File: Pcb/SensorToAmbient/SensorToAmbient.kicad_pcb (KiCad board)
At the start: 2 copper layers, 161.9 x 69.7 mm, 17 parts, among them J1 Conn_01x04, J2 Conn_01x04, J3 Conn_01x04, J4 Conn_01x04, J5 Conn_01x04, J6 Conn_01x04, J7 Conn_01x02, J8 Conn_01x06, J9 Conn_01x06

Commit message: Commit intermediate (Delete Wil LTE outline from pcb)
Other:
- board size 161.9 x 69.7 mm -> 48.1 x 69.7 mm
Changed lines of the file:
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@@
   (general
     (thickness 1.6)
-    (drawings 18)
+    (drawings 10)
     (tracks 198)
     (zones 0)
@@
     (add_net GND)
   )
+  (module SensorToAmbient:RTC-8564NB_Akiduki (layer F.Cu)
+    (at 48.58 42.39)
+    (descr http://media.digikey.com/pdf/Data%20Sheets/Lite-On%20PDFs/6N137%20Series.pdf)
+    (fp_text reference RTC1 (at 4.05 -2.52) (layer F.SilkS)
+      (effects (font (size 1 1) (thickness 0.15)))
+    )
+    (fp_text value RTC-8564NB (at 3.94 12.954) (layer F.Fab)
+      (effects (font (size 1 1) (thickness 0.15)))
+    )
+    (fp_line (start -1.05 11.89) (end 8.67 11.89) (layer F.SilkS) (width 0.1))
+    (fp_line (start -1.05 -4.29) (end -1.05 11.89) (layer F.SilkS) (width 0.1))
+    (fp_line (start 8.67 -4.29) (end 8.67 11.89) (layer F.SilkS) (width 0.1))
+    (fp_line (start -1.05 -4.29) (end 8.67 -4.29) (layer F.SilkS) (width 0.1))
+    (fp_line (start 0.4 -0.9) (end 0.4 -1.2) (layer F.SilkS) (width 0.1))
+    (fp_line (start 0.4 -1.2) (end 0.7 -1.2) (layer F.SilkS) (width 0.1))
+    (fp_line (start 7.2 -0.9) (end 7.2 -1.2) (layer F.SilkS) (width 0.1))
+    (fp_line (start 7.2 -1.2) (end 6.9 -1.2) (layer F.SilkS) (width 0.1))
+    (fp_line (start 7.2 8.5) (end 7.2 8.8) (layer F.SilkS) (width 0.1))
+    (fp_line (start 7.2 8.8) (end 6.9 8.8) (layer F.SilkS) (width 0.1))
+    (fp_line (start 0.4 8.5) (end 0.4 8.8) (layer F.SilkS) (width 0.1))
+    (fp_line (start 0.4 8.8) (end 0.7 8.8) (layer F.SilkS) (width 0.1))
+    (fp_line (start 0.55 8.64) (end 7.05 8.64) (layer F.Fab) (width 0.1))
+    (fp_line (start 0.55 -1.04) (end 7.05 -1.04) (layer F.Fab) (width 0.1))
+    (fp_line (start 7.05 -1.04) (end 7.05 8.64) (layer F.Fab) (width 0.1))
+    (fp_line (start 0.55 -1.04) (end 0.55 8.64) (layer F.Fab) (width 0.1))
+    (fp_text user REF** (at 3.94 3.49) (layer F.Fab)
+      (effects (font (size 1 1) (thickness 0.1)))
+    )
+    (pad 1 thru_hole rect (at 0 0) (size 1.6 1.6) (drill 1) (layers *.Cu *.Mask)
+      (net 34 "Net-(RTC1-Pad1)"))
+    (pad 2 thru_hole circle (at 0 2.54) (size 1.6 1.6) (drill 1) (layers *.Cu *.Mask)
+      (net 16 "Net-(J2-Pad4)"))
+    (pad 3 thru_hole circle (at 0 5.08) (size 1.6 1.6) (drill 1) (layers *.Cu *.Mask)
+      (net 12 "Net-(DCDC1-Pad3)"))
+    (pad 4 thru_hole circle (at 0 7.62) (size 1.6 1.6) (drill 1) (layers *.Cu *.Mask)
+      (net 6 GND))
+    (pad 8 thru_hole circle (at 7.62 7.62) (size 1.6 1.6) (drill 1) (layers *.Cu *.Mask)
+      (net 19 /PWR_BAT))
+    (pad 7 thru_hole circle (at 7.62 5.08) (size 1.6 1.6) (drill 1) (layers *.Cu *.Mask)
+      (net 18 "Net-(RTC1-Pad7)"))
+    (pad 6 thru_hole circle (at 7.62 2.54) (size 1.6 1.6) (drill 1) (layers *.Cu *.Mask)
+      (net 20 "Net-(J5-Pad4)"))
+    (pad 5 thru_hole circle (at 7.62 0) (size 1.6 1.6) (drill 1) (layers *.Cu *.Mask)
+      (net 21 "Net-(J5-Pad3)"))
+    (model ${KIPRJMOD}/RTC-8564NB_Akidsuki.wrl
+      (at (xyz 0 0 0))
+      (scale (xyz 0.394 0.394 0.394))
+      (rotate (xyz -90 0 0))
+    )
+  )
   (module SensorToAmbient:DCDC_PowerBoost500 (layer F.Cu)
     (at 46.28 73.08 270)
@@
       (net 19 /PWR_BAT))
     (model ${KIPRJMOD}/PowerBoost500.wrl
-      (at (xyz 0 0 0))
-      (scale (xyz 0.394 0.394 0.394))
-      (rotate (xyz -90 0 0))
-    )
-  )
-  (module SensorToAmbient:RTC-8564NB_Akiduki (layer F.Cu)
-    (at 48.58 42.39)
-    (descr http://media.digikey.com/pdf/Data%20Sheets/Lite-On%20PDFs/6N137%20Series.pdf)
-    (fp_text reference RTC1 (at 4.05 -2.52) (layer F.SilkS)
-      (effects (font (size 1 1) (thickness 0.15)))
-    )
-    (fp_text value RTC-8564NB (at 3.94 12.954) (layer F.Fab)
-      (effects (font (size 1 1) (thickness 0.15)))
-    )
-    (fp_text user REF** (at 3.94 3.49) (layer F.Fab)
-      (effects (font (size 1 1) (thickness 0.1)))
-    )
-    (fp_line (start 0.55 -1.04) (end 0.55 8.64) (layer F.Fab) (width 0.1))
-    (fp_line (start 7.05 -1.04) (end 7.05 8.64) (layer F.Fab) (width 0.1))
-    (fp_line (start 0.55 -1.04) (end 7.05 -1.04) (layer F.Fab) (width 0.1))
-    (fp_line (start 0.55 8.64) (end 7.05 8.64) (layer F.Fab) (width 0.1))
-    (fp_line (start 0.4 8.8) (end 0.7 8.8) (layer F.SilkS) (width 0.1))
-    (fp_line (start 0.4 8.5) (end 0.4 8.8) (layer F.SilkS) (width 0.1))
-    (fp_line (start 7.2 8.8) (end 6.9 8.8) (layer F.SilkS) (width 0.1))
-    (fp_line (start 7.2 8.5) (end 7.2 8.8) (layer F.SilkS) (width 0.1))
-    (fp_line (start 7.2 -1.2) (end 6.9 -1.2) (layer F.SilkS) (width 0.1))
-    (fp_line (start 7.2 -0.9) (end 7.2 -1.2) (layer F.SilkS) (width 0.1))
-    (fp_line (start 0.4 -1.2) (end 0.7 -1.2) (layer F.SilkS) (width 0.1))
-    (fp_line (start 0.4 -0.9) (end 0.4 -1.2) (layer F.SilkS) (width 0.1))
-    (fp_line (start -1.05 -4.29) (end 8.67 -4.29) (layer F.SilkS) (width 0.1))
-    (fp_line (start 8.67 -4.29) (end 8.67 11.89) (layer F.SilkS) (width 0.1))
-    (fp_line (start -1.05 -4.29) (end -1.05 11.89) (layer F.SilkS) (width 0.1))
-    (fp_line (start -1.05 11.89) (end 8.67 11.89) (layer F.SilkS) (width 0.1))
-    (pad 5 thru_hole circle (at 7.62 0) (size 1.6 1.6) (drill 1) (layers *.Cu *.Mask)
-      (net 21 "Net-(J5-Pad3)"))
-    (pad 6 thru_hole circle (at 7.62 2.54) (size 1.6 1.6) (drill 1) (layers *.Cu *.Mask)
-      (net 20 "Net-(J5-Pad4)"))
-    (pad 7 thru_hole circle (at 7.62 5.08) (size 1.6 1.6) (drill 1) (layers *.Cu *.Mask)
-      (net 18 "Net-(RTC1-Pad7)"))
-    (pad 8 thru_hole circle (at 7.62 7.62) (size 1.6 1.6) (drill 1) (layers *.Cu *.Mask)
-      (net 19 /PWR_BAT))
-    (pad 4 thru_hole circle (at 0 7.62) (size 1.6 1.6) (drill 1) (layers *.Cu *.Mask)
-      (net 6 GND))
-    (pad 3 thru_hole circle (at 0 5.08) (size 1.6 1.6) (drill 1) (layers *.Cu *.Mask)
-      (net 12 "Net-(DCDC1-Pad3)"))
-    (pad 2 thru_hole circle (at 0 2.54) (size 1.6 1.6) (drill 1) (layers *.Cu *.Mask)
-      (net 16 "Net-(J2-Pad4)"))
-    (pad 1 thru_hole rect (at 0 0) (size 1.6 1.6) (drill 1) (layers *.Cu *.Mask)
-      (net 34 "Net-(RTC1-Pad1)"))
-    (model D:/sonatine726/Work/PaddyFieldAutoGate/3D_Model/RTC-8564NB_Akidsuki/RTC-8564NB_Akidsuki.wrl
       (at (xyz 0 0 0))
       (scale (xyz 0.394 0.394 0.394))
@@
     (effects (font (size 1.5 1.5) (thickness 0.3)))
   )
-  (gr_arc (start 179.823 75.947) (end 179.823 80.727) (angle -90) (layer Edge.Cuts) (width 0.2))
-  (gr_line (start 141.25 80.727) (end 179.823 80.727) (layer Edge.Cuts) (width 0.2))
-  (gr_line (start 141.25 26) (end 179.823 26) (layer Edge.Cuts) (width 0.2))
-  (gr_arc (start 141.25 75.947) (end 136.47 75.947) (angle -90) (layer Edge.Cuts) (width 0.2))
-  (gr_arc (start 179.823 30.78) (end 179.823 26) (angle 90) (layer Edge.Cuts) (width 0.2))
-  (gr_line (start 184.603 30.78) (end 184.603 75.947) (layer Edge.Cuts) (width 0.2))
-  (gr_arc (start 141.25 30.78) (end 141.25 26) (angle -90) (layer Edge.Cuts) (width 0.2))
-  (gr_line (start 136.47 30.78) (end 136.47 75.947) (layer Edge.Cuts) (width 0.2))
   (gr_arc (start 66.023 82.727) (end 66.023 87.507) (angle -90) (layer Edge.Cuts) (width 0.2))
   (gr_line (start 27.45 87.507) (end 66.023 87.507) (layer Edge.Cuts) (width 0.2))

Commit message: Commit intermediate (Making double-side board)
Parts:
- added D1: D_Schottky, Diodes_THT:D_T-1_P5.08mm_Horizontal, F.Cu at (36.6, 76.5)
- added R3: R, Resistors_THT:R_Axial_DIN0207_L6.3mm_D2.5mm_P7.62mm_Horizontal, F.Cu at (38.1, 72.6)
- added R4: R, Resistors_THT:R_Axial_DIN0207_L6.3mm_D2.5mm_P7.62mm_Horizontal, F.Cu at (25.9, 50.3)
- added REF**: MountingHole_3mm_rev, SensorToAmbient:MountingHole_3mm_rev, F.Cu at (67.4, 84.6)
- added REF**: MountingHole_3mm_rev, SensorToAmbient:MountingHole_3mm_rev, F.Cu at (26.2, 35.7)
- added SW1: SW_Push, Connectors_JST:JST_XH_S02B-XH-A_02x2.50mm_Angled, F.Cu at (34.0, 81.8)
- added SW2: SW_Push, Connectors_JST:JST_XH_S02B-XH-A_02x2.50mm_Angled, F.Cu at (29.2, 27.4)
- J7: footprint Connectors_JST:JST_XH_S02B-XH-A_02x2.50mm_Angled -> Connectors_JST:JST_PH_S2B-PH-K_02x2.00mm_Angled
- moved G*** 30.9 mm to (85.3, 25.1)
- moved J8 8.00 mm to (42.5, 19.6)
- moved J9 8.00 mm to (63.2, 19.6)
- moved J7 4.63 mm to (45.0, 82.8)
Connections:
- 3SB1 pad 14: /PWR3.3V -> /PWR_BAT
- 3SB1 pad 2: Net-(3SB1-Pad2) -> /PWR_BAT
- 3SB1 pad 3: Net-(3SB1-Pad3) -> /PWR3.3V
- DCDC1 pad 3: Net-(DCDC1-Pad3) -> /PWR3.3V
- J1 pad 2: Net-(J1-Pad2) -> /PWR3.3V
- RTC1 pad 3: Net-(DCDC1-Pad3) -> Net-(3SB1-Pad1)
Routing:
- net GND: track 290.1 -> 88.4 mm
- net Net-(DCDC1-Pad3): track 73.7 -> 0.00 mm
- net Net-(J1-Pad4): track 0.00 -> 24.3 mm
- net Net-(J2-Pad4): track 96.9 -> 114.3 mm
- net Net-(J2-Pad3): track 58.6 -> 71.2 mm
- net Net-(3SB1-Pad12): track 21.2 -> 29.2 mm
- net Net-(3SB1-Pad1): track 0.00 -> 6.73 mm
- net /PWR3.3V: track 124.5 -> 131.2 mm
- net Net-(D1-Pad1): track 0.00 -> 5.37 mm
- net Net-(3SB1-Pad9): track 21.9 -> 27.0 mm
- net Net-(J3-Pad3): track 96.9 -> 100.4 mm
- net /PWR_BAT: track 101.0 -> 104.3 mm
- net Net-(3SB1-Pad10): track 41.2 -> 42.8 mm
- net /PWR5V: track 30.3 -> 28.9 mm
- net Net-(J5-Pad3): track 22.7 -> 21.7 mm
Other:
- board size 48.1 x 69.7 mm -> 48.1 x 77.7 mm

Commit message: Complete making new double-side board
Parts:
- added D2: D_Schottky, Diodes_THT:D_T-1_P5.08mm_Horizontal, F.Cu at (43.2, 58.7)
- moved G*** 40.0 mm to (45.5, 28.0)
- moved R3 12.5 mm to (50.5, 73.9), turned to 180 degrees
- moved D1 7.52 mm to (43.9, 78.0)
- moved R1 0.72 mm to (50.5, 69.1)
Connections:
- 3SB1 pad 3: /PWR3.3V -> Net-(3SB1-Pad3)
- DCDC1 pad 3: /PWR3.3V -> /PWR3.3V_DCDC
- J1 pad 2: /PWR3.3V -> /PWR3.3V_Sensor
- J3 pad 1: GND -> Net-(J3-Pad1)
- J3 pad 2: /PWR3.3V -> Net-(J3-Pad2)
- J4 pad 2: Net-(J4-Pad2) -> /PWR3.3V_DCDC
- J8 pad 1: /PWR3.3V -> /PWR3.3V_Sensor
- J9 pad 1: /PWR3.3V -> /PWR3.3V_Sensor
- R3 pad 1: /PWR3.3V -> /PWR3.3V_DCDC
- SW1 pad 1: /PWR3.3V -> /PWR3.3V_DCDC
- SW2 pad 1: /PWR3.3V -> /PWR3.3V_Sensor
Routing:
- net /PWR3.3V: track 131.2 -> 0.00 mm
- net GND: track 88.4 -> 194.8 mm
- net /PWR3.3V_Sensor: track 0.00 -> 62.8 mm
- net /PWR3.3V_DCDC: track 0.00 -> 57.4 mm
- net Net-(3SB1-Pad3): track 0.00 -> 13.3 mm
- net Net-(D1-Pad1): track 5.37 -> 9.05 mm
- net /PWR_BAT: track 104.3 -> 105.6 mm
- net Net-(3SB1-Pad4): track 1.13 -> 0.00 mm
- net /PWR5V: track 28.9 -> 27.9 mm
- added copper zone on F.Cu, net GND
- removed copper zone on B.Cu, net GND

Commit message: Commit intermediate (Complete of fixing schmatic)
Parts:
- added R5: 47K, Resistors_THT:R_Axial_DIN0207_L6.3mm_D2.5mm_P7.62mm_Horizontal, F.Cu at (79.5, 60.2)
- added R6: 47K, Resistors_THT:R_Axial_DIN0207_L6.3mm_D2.5mm_P7.62mm_Horizontal, F.Cu at (75.7, 71.4)
- added R7: 47K, Resistors_THT:R_Axial_DIN0207_L6.3mm_D2.5mm_P7.62mm_Horizontal, F.Cu at (55.9, 94.5)
- added R8: 4.7K, Resistors_THT:R_Axial_DIN0207_L6.3mm_D2.5mm_P7.62mm_Horizontal, F.Cu at (80.5, 38.1)
- added R9: 4.7K, Resistors_THT:R_Axial_DIN0207_L6.3mm_D2.5mm_P7.62mm_Horizontal, F.Cu at (84.6, 29.5)
- R3: value R -> 47K
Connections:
- D1 pad 2: /PWR_BAT -> Net-(D1-Pad2)
- D2 pad 1: /PWR3.3V_DCDC -> Net-(D2-Pad1)
- DCDC1 pad 3: /PWR3.3V_DCDC -> Net-(D2-Pad1)
- J1 pad 2: /PWR3.3V_Sensor -> /PWR3.3V_Switch
- J6 pad 2: Net-(J6-Pad2) -> /PWR3.3V_Sensors
- J8 pad 1: /PWR3.3V_Sensor -> /PWR3.3V_Sensors
- J9 pad 1: /PWR3.3V_Sensor -> /PWR3.3V_Sensors
- R3 pad 1: /PWR3.3V_DCDC -> Net-(D2-Pad1)
- RTC1 pad 5: Net-(J5-Pad3) -> Net-(RTC1-Pad5)
- RTC1 pad 6: Net-(J5-Pad4) -> Net-(RTC1-Pad6)
- SW1 pad 1: /PWR3.3V_DCDC -> Net-(D2-Pad1)
- SW2 pad 1: /PWR3.3V_Sensor -> /PWR3.3V_Switch

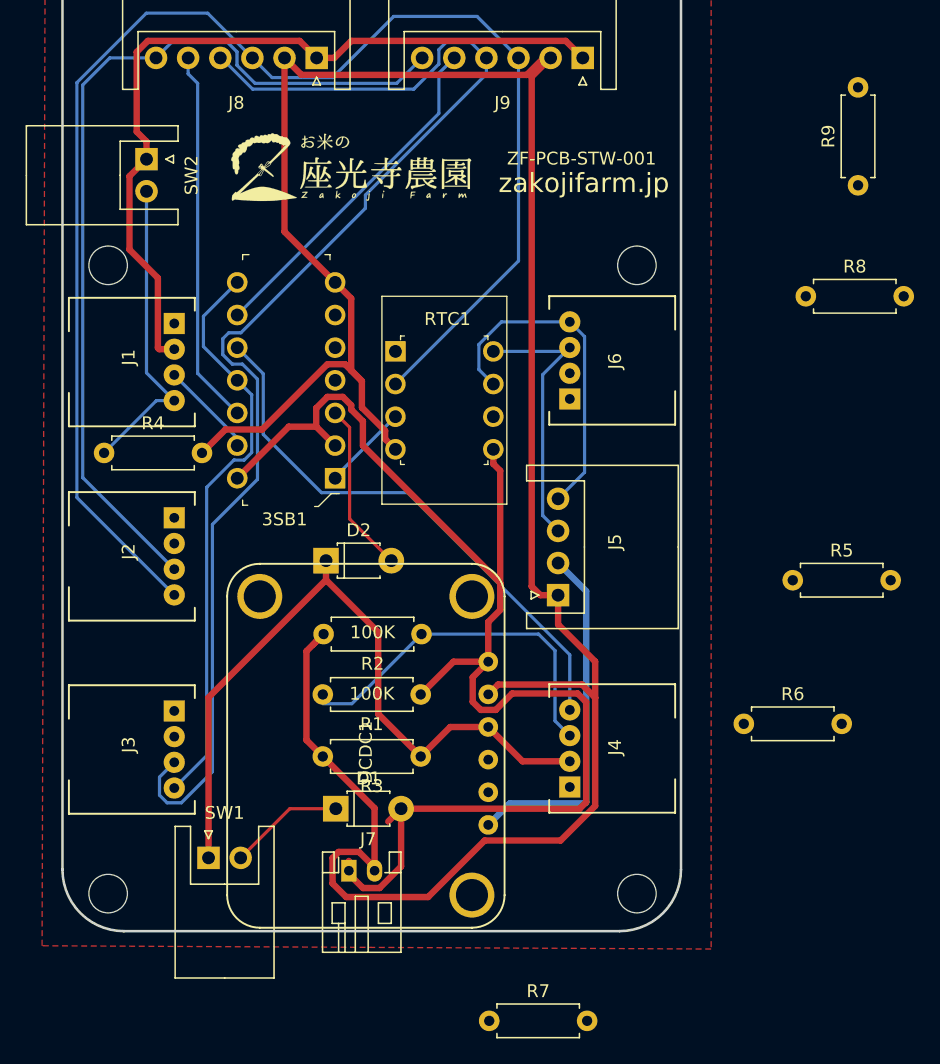
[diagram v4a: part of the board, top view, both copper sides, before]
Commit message: Commit intermediate (Changing footprints of resistor and diode to SMD)
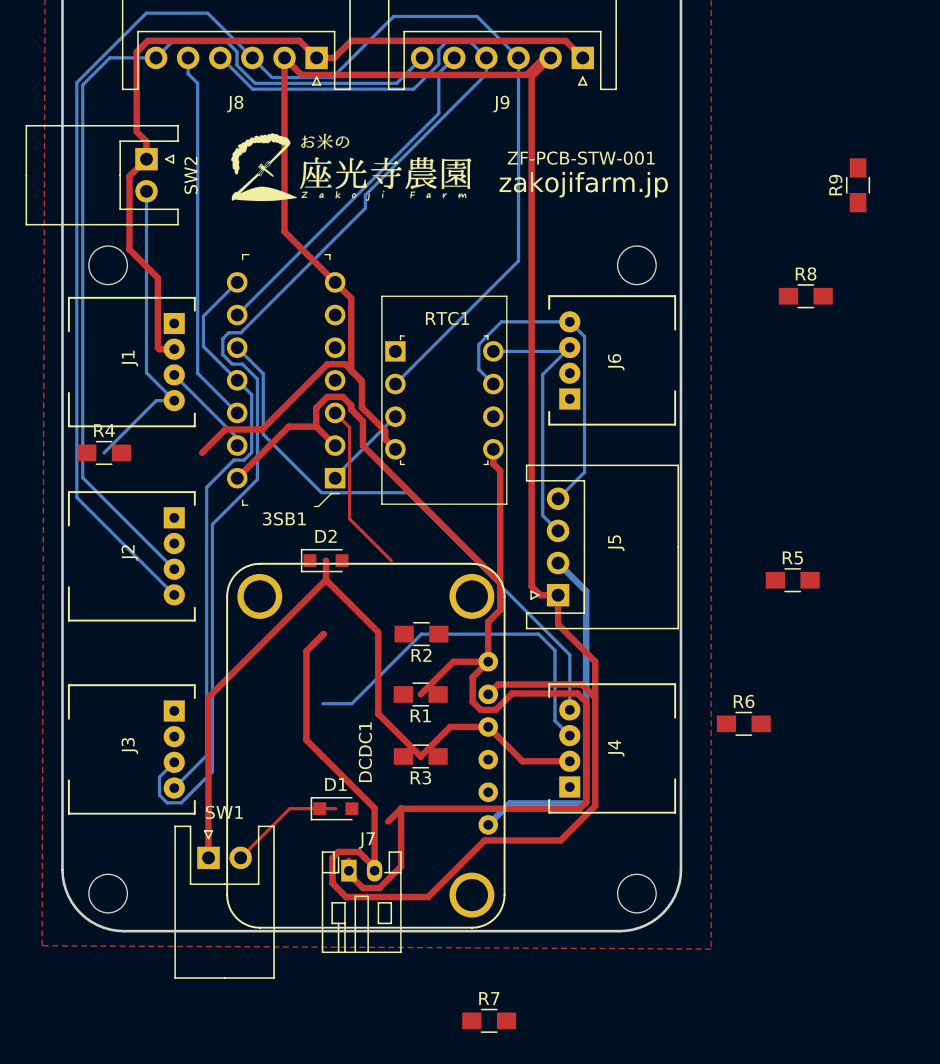
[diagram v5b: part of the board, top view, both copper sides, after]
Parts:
- D1, D2: footprint Diodes_THT:D_T-1_P5.08mm_Horizontal -> Diodes_SMD:D_SOD-323_HandSoldering
- R1, R2, R3, R4, R5, R6, R7, R8, R9: footprint Resistors_THT:R_Axial_DIN0207_L6.3mm_D2.5mm_P7.62mm_Horizontal -> Resistors_SMD:R_0805_HandSoldering

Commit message: Commit intermediate ( First complete of updating pcb )
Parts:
- moved R5 36.3 mm to (52.4, 36.0)
- moved R9 22.6 mm to (62.1, 32.2), turned to 0 degrees
- moved R7 20.5 mm to (46.0, 76.5), turned to 180 degrees
- moved R4 20.2 mm to (35.9, 32.8)
- moved R8 18.6 mm to (62.1, 35.5)
- moved R6 16.8 mm to (59.0, 72.9), turned to 90 degrees
- moved D2 10.0 mm to (41.2, 68.5), turned to 90 degrees
- moved R3 8.47 mm to (44.2, 68.2), turned to 90 degrees
- moved R2 4.96 mm to (47.5, 68.2), turned to 90 degrees
- moved D1 4.21 mm to (40.0, 76.5)
- moved R1 0.95 mm to (51.0, 68.2), turned to 90 degrees
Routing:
- net /PWR3.3V_Sensor: track 62.8 -> 0.00 mm
- net /PWR3.3V_DCDC: track 57.4 -> 3.22 mm
- net /PWR3.3V_Sensors: track 0.00 -> 47.9 mm
- net Net-(D2-Pad1): track 0.00 -> 33.7 mm
- net /PWR3.3V_Switch: track 0.00 -> 17.5 mm
- net GND: track 194.8 -> 209.6 mm
- net Net-(3SB1-Pad1): track 6.73 -> 19.2 mm
- net Net-(J5-Pad3): track 21.7 -> 33.0 mm
- net /PWR_BAT: track 105.6 -> 116.3 mm
- net Net-(J4-Pad3): track 27.9 -> 18.2 mm, vias 0 -> 1
- net Net-(3SB1-Pad3): track 13.3 -> 22.1 mm
- net Net-(J5-Pad4): track 26.4 -> 31.6 mm
- net Net-(D1-Pad2): track 0.00 -> 3.40 mm
- net Net-(D1-Pad1): track 9.05 -> 6.72 mm
- net Net-(J1-Pad4): track 24.3 -> 23.7 mm
- removed copper zone on F.Cu, net GND

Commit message: Complete fixing pcb board
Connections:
- RTC1 pad 5: Net-(RTC1-Pad5) -> Net-(J5-Pad3)
- RTC1 pad 6: Net-(RTC1-Pad6) -> Net-(J5-Pad4)
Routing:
- net Net-(J5-Pad3): track 33.0 -> 37.7 mm
- net Net-(J5-Pad4): track 31.6 -> 30.1 mm
- net /PWR_BAT: track 116.3 -> 117.0 mm
- added copper zone on F.Cu, net GND
